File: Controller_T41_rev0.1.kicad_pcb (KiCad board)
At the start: 2 copper layers, 23 parts, among them J1 RJ45, J2 RJ45, J3 RJ45, J4 RJ45, J5 RJ45, J6 RJ45, J7 RJ45, J8 RJ45, J9 Screw_Terminal_01x02, U1 74HC245, U2 74HC245, U3 Teensy4.1, U4 74HC245, U5 74HC245

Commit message: Changes to be committed: 	modified:   Controller_T41_rev0.1.kicad_pcb 	modified:   Controller_T41_rev0.1.kicad_pcb-bak
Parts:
- moved H1 31.8 mm to (143.3, 97.4)
- moved H2 31.8 mm to (143.3, 148.1)
- moved H3 31.8 mm to (168.7, 97.4)
- moved H4 31.8 mm to (168.7, 148.2)
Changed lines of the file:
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@@
   )
   (module MountingHole:MountingHole_3mm_Pad_Via (layer F.Cu)
-    (at 175.006 97.028)
+    (at 143.256 97.409)
     (descr "Mounting Hole 3mm")
     (tags "mounting hole 3mm")
@@
   )
   (module MountingHole:MountingHole_3mm_Pad_Via (layer F.Cu)
-    (at 175.006 147.701)
+    (at 143.256 148.082)
     (descr "Mounting Hole 3mm")
     (tags "mounting hole 3mm")
@@
   )
   (module MountingHole:MountingHole_3mm_Pad_Via (layer F.Cu)
-    (at 200.406 97.028)
+    (at 168.656 97.409)
     (descr "Mounting Hole 3mm")
     (tags "mounting hole 3mm")
@@
   )
   (module MountingHole:MountingHole_3mm_Pad_Via (layer F.Cu)
-    (at 200.406 147.828)
+    (at 168.656 148.209)
     (descr "Mounting Hole 3mm")
     (tags "mounting hole 3mm")

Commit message: modified:   Controller_T41_rev0.1.kicad_pcb 	modified:   Controller_T41_rev0.1.kicad_pcb-bak 	modified:   Controller_T41_rev0.1.net 	modified:   Controller_T41_rev0.1.sch-bak 	modified:   fp-info-cache
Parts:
- moved J4 179.1 mm to (172.3, 39.5), turned to 180 degrees
- moved J3 156.4 mm to (154.2, 39.5), turned to 180 degrees
- moved J8 148.9 mm to (172.3, 192.8), turned to 0 degrees
- moved J2 127.2 mm to (185.8, 91.4), turned to 90 degrees
- moved J7 125.7 mm to (155.1, 192.8), turned to 0 degrees
- moved RN3 119.7 mm to (175.4, 154.6), turned to 270 degrees
- moved J6 113.8 mm to (185.8, 163.3), turned to 90 degrees
- moved J1 102.6 mm to (185.8, 108.7), turned to 90 degrees
- moved RN4 97.0 mm to (147.4, 153.4), turned to 270 degrees
- moved U4 95.0 mm to (155.1, 142.5), turned to 90 degrees
- moved J5 89.7 mm to (185.8, 146.1), turned to 90 degrees
- moved U2 88.1 mm to (177.9, 102.9), turned to 270 degrees
- moved RN2 87.0 mm to (175.4, 84.7), turned to 270 degrees
- moved U5 78.2 mm to (127.1, 142.5), turned to 90 degrees
- moved U3 73.4 mm to (156.1, 122.9), turned to 180 degrees
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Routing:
- net GND: track 389.7 -> 0.00 mm
- net Net-(C1-Pad2): track 174.2 -> 0.00 mm
- net Net-(J4-Pad2): track 117.0 -> 0.00 mm
- net Net-(J4-Pad4): track 112.6 -> 0.00 mm
- net Net-(J4-Pad6): track 107.9 -> 0.00 mm
- net Net-(J5-Pad2): track 107.8 -> 0.00 mm
- net Net-(J4-Pad8): track 103.5 -> 0.00 mm
- net Net-(J5-Pad4): track 103.1 -> 0.00 mm
- net Net-(J5-Pad6): track 98.4 -> 0.00 mm
- net Net-(J5-Pad8): track 93.7 -> 0.00 mm
- net Net-(J3-Pad2): track 90.7 -> 0.00 mm
- net Net-(J6-Pad2): track 86.3 -> 0.00 mm
- net Net-(J3-Pad4): track 86.0 -> 0.00 mm
- net Net-(J6-Pad4): track 81.6 -> 0.00 mm
- net Net-(J3-Pad6): track 81.3 -> 0.00 mm
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
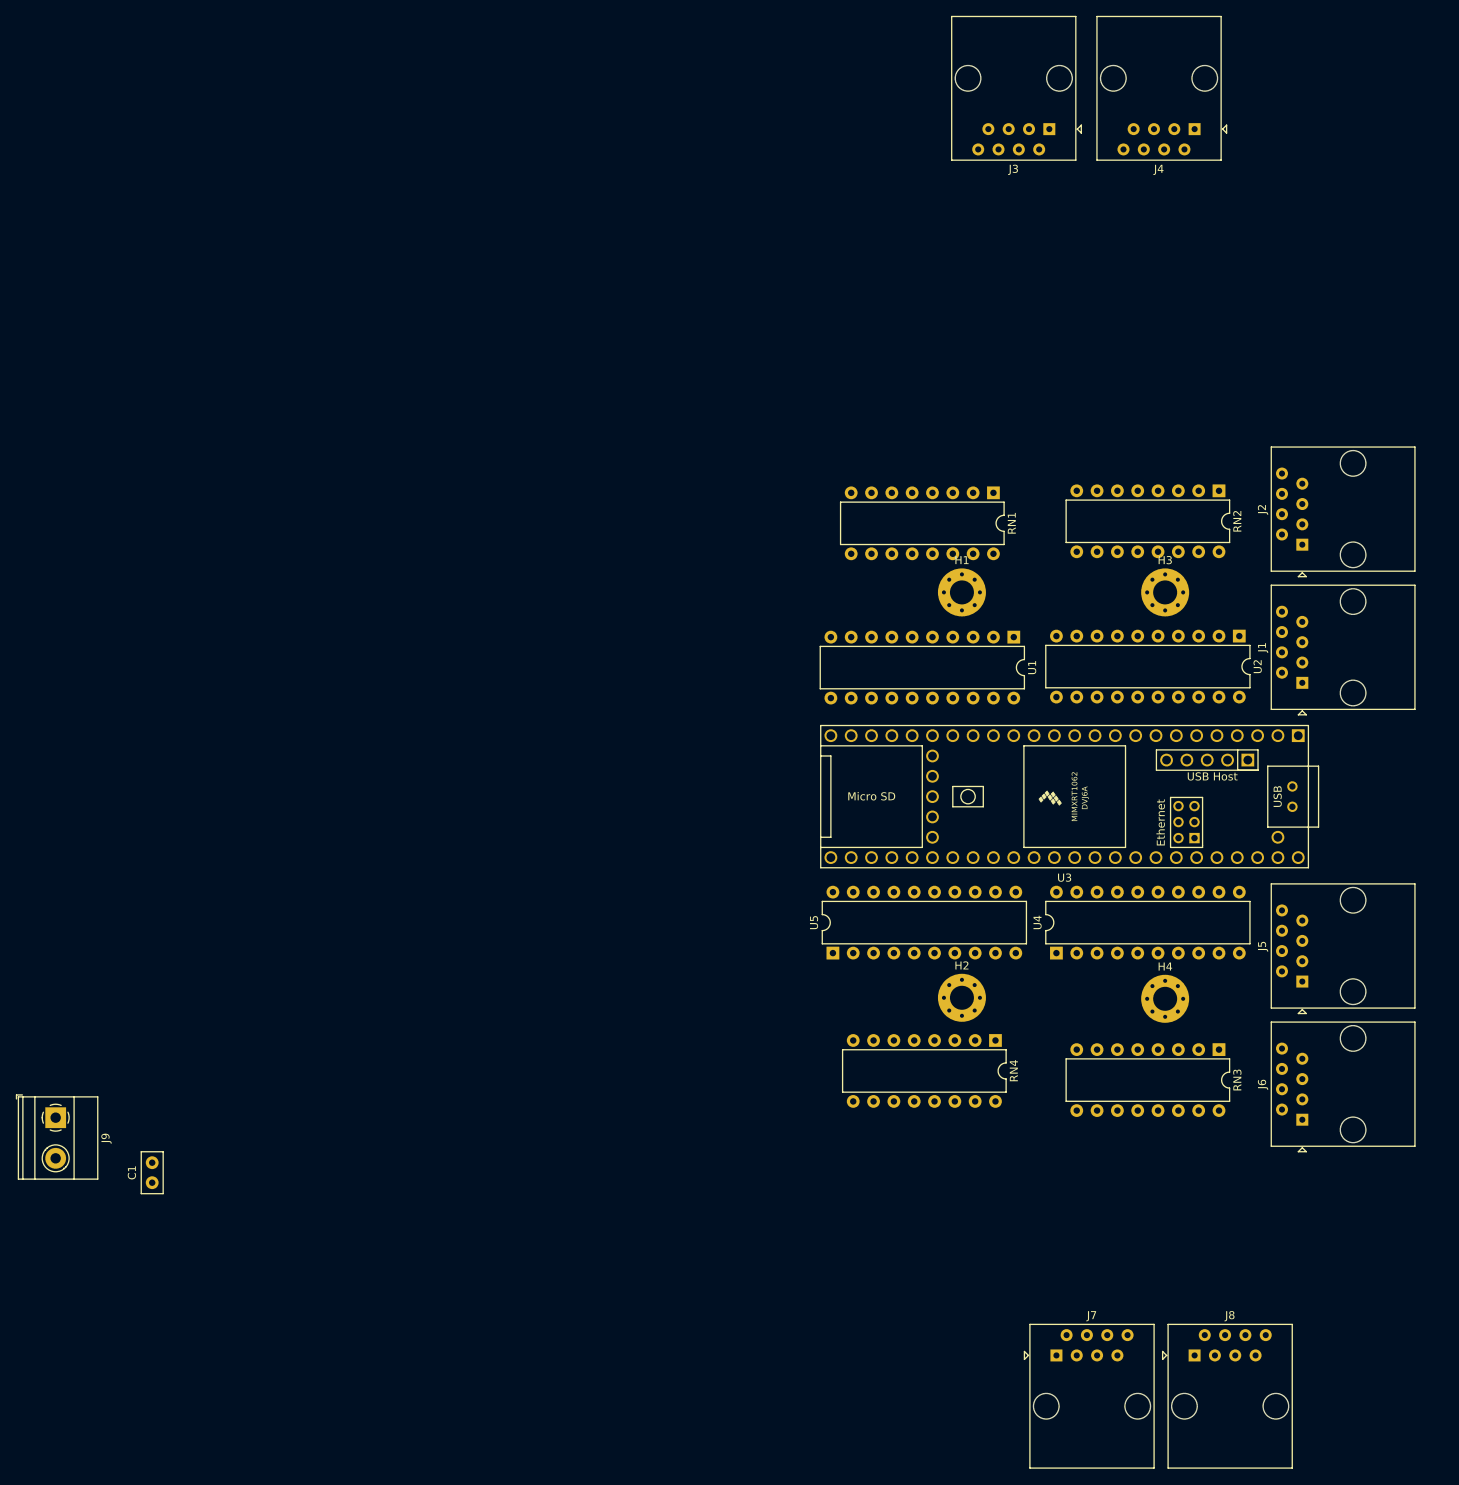
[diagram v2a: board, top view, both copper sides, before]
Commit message: updated board layout, converted rj-45 ports to dual rj-45 ports Converted design to kicad 5.
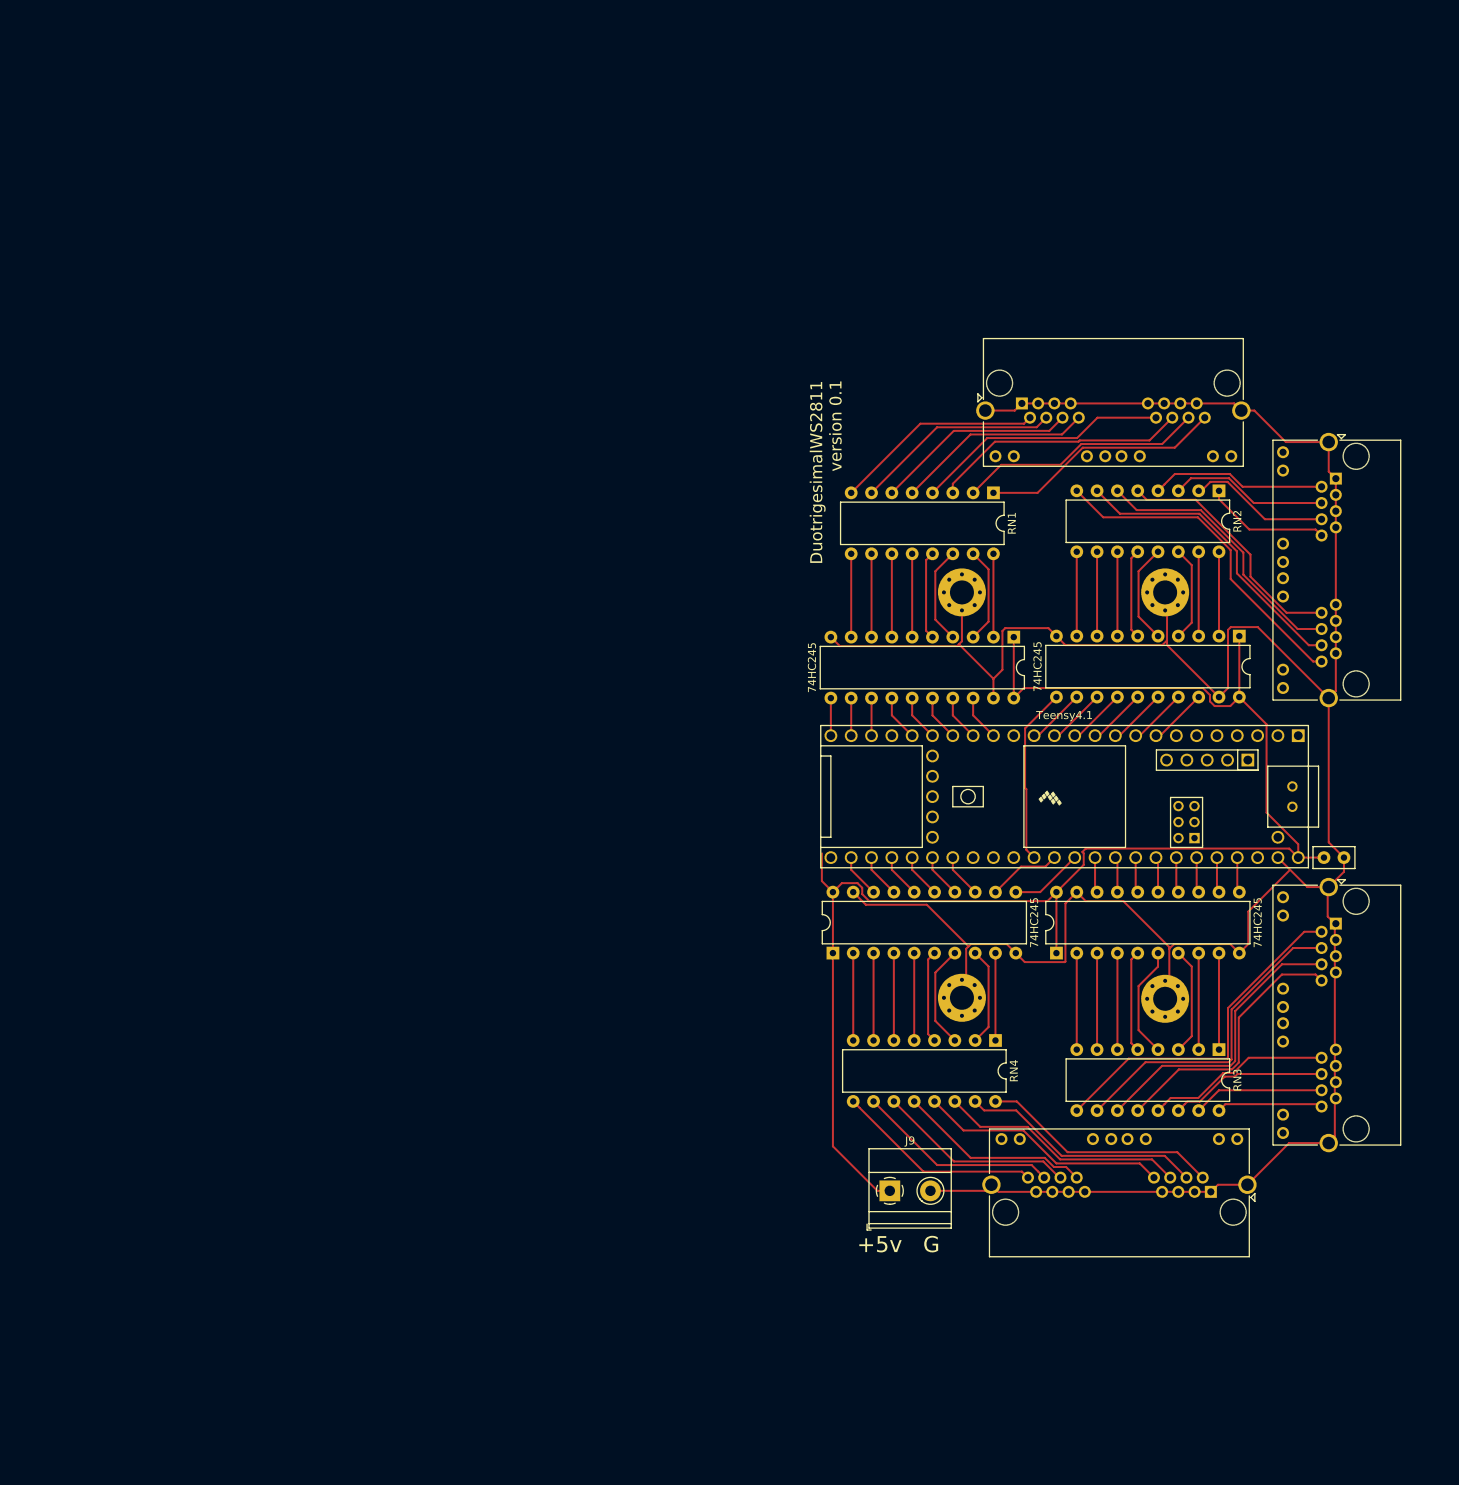
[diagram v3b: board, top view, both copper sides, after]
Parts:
- removed J5, J6, J7, J8: RJ45, Connector_RJ:RJ45_Amphenol_54602-x08_Horizontal
- J1, J2, J3, J4: value RJ45 -> RJ45_LED_Shielded_x2; footprint Connector_RJ:RJ45_Amphenol_54602-x08_Horizontal -> Connector_RJ:RJ45_Amphenol_RJHSE538X-02
- moved C1 154.4 mm to (191.0, 130.6), turned to 180 degrees
- moved J3 134.4 mm to (174.4, 172.3)
- moved J9 104.7 mm to (134.2, 172.2), turned to 0 degrees
- moved J4 100.9 mm to (190.0, 138.8), turned to 270 degrees
- moved J2 39.2 mm to (150.7, 73.8), turned to 0 degrees
- moved J1 25.9 mm to (190.0, 83.2), turned to 270 degrees
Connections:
- H2 pad 1: Net-(H2-Pad1) -> GND
- J1 pad 8: Net-(H2-Pad1) -> Net-(J1-Pad8)
- RN1 pad 1: Net-(J3-Pad8) -> Net-(J2-Pad20)
- RN1 pad 2: Net-(J3-Pad6) -> Net-(J2-Pad18)
- RN1 pad 3: Net-(J3-Pad4) -> Net-(J2-Pad16)
- RN1 pad 4: Net-(J3-Pad2) -> Net-(J2-Pad14)
- RN1 pad 5: Net-(J4-Pad8) -> Net-(J2-Pad8)
- RN1 pad 6: Net-(J4-Pad6) -> Net-(J2-Pad6)
- RN1 pad 7: Net-(J4-Pad4) -> Net-(J2-Pad4)
- RN1 pad 8: Net-(J4-Pad2) -> Net-(J2-Pad2)
- RN2 pad 1: Net-(H2-Pad1) -> Net-(J1-Pad8)
- RN2 pad 5: Net-(J2-Pad8) -> Net-(J1-Pad14)
- RN2 pad 6: Net-(J2-Pad6) -> Net-(J1-Pad16)
- RN2 pad 7: Net-(J2-Pad4) -> Net-(J1-Pad18)
- RN2 pad 8: Net-(J2-Pad2) -> Net-(J1-Pad20)
- RN3 pad 10: Net-(J6-Pad6) -> Net-(J4-Pad4)
- RN3 pad 11: Net-(J6-Pad4) -> Net-(J4-Pad6)
- RN3 pad 12: Net-(J6-Pad2) -> Net-(J4-Pad8)
- RN3 pad 13: Net-(J5-Pad8) -> Net-(J4-Pad14)
- RN3 pad 14: Net-(J5-Pad6) -> Net-(J4-Pad16)
- RN3 pad 15: Net-(J5-Pad4) -> Net-(J4-Pad18)
- RN3 pad 16: Net-(J5-Pad2) -> Net-(J4-Pad20)
- RN3 pad 9: Net-(J6-Pad8) -> Net-(J4-Pad2)
- RN4 pad 10: Net-(J8-Pad6) -> Net-(J3-Pad18)
- RN4 pad 11: Net-(J8-Pad4) -> Net-(J3-Pad16)
- RN4 pad 12: Net-(J8-Pad2) -> Net-(J3-Pad14)
- RN4 pad 13: Net-(J7-Pad8) -> Net-(J3-Pad8)
- RN4 pad 14: Net-(J7-Pad6) -> Net-(J3-Pad6)
- RN4 pad 15: Net-(J7-Pad4) -> Net-(J3-Pad4)
- RN4 pad 16: Net-(J7-Pad2) -> Net-(J3-Pad2)
- RN4 pad 9: Net-(J8-Pad8) -> Net-(J3-Pad20)
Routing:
- net GND: track 0.00 -> 387.8 mm
- net Net-(C1-Pad2): track 0.00 -> 190.8 mm
- net Net-(J4-Pad2): track 0.00 -> 43.5 mm
- net Net-(J1-Pad20): track 0.00 -> 41.6 mm
- net Net-(J4-Pad4): track 0.00 -> 40.1 mm
- net Net-(J1-Pad18): track 0.00 -> 37.7 mm
- net Net-(J4-Pad6): track 0.00 -> 36.8 mm
- net Net-(J1-Pad16): track 0.00 -> 34.3 mm
- net Net-(J4-Pad8): track 0.00 -> 33.6 mm
- net Net-(J2-Pad16): track 0.00 -> 32.0 mm
- net Net-(J2-Pad14): track 0.00 -> 31.8 mm
- net Net-(J3-Pad8): track 0.00 -> 31.4 mm
- net Net-(J1-Pad14): track 0.00 -> 30.9 mm
- net Net-(J3-Pad6): track 0.00 -> 30.9 mm
- net Net-(J2-Pad18): track 0.00 -> 30.8 mm
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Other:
- board text added: "+5v"
- board text added: "DuotrigesimalWS2811"
- board text added: "G"
- board text added: "version 0.1"

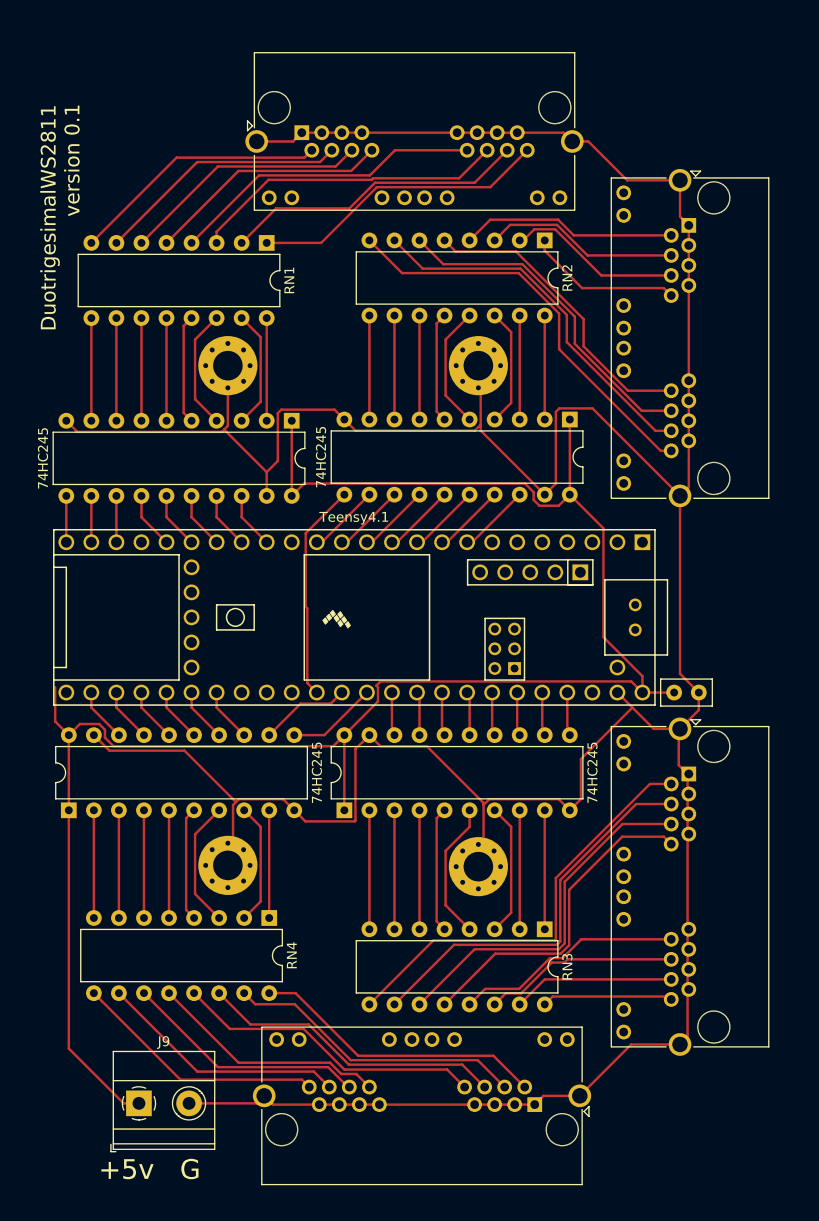
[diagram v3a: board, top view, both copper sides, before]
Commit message: modified:   Controller_T41_rev0.1.kicad_pcb Added board outline.
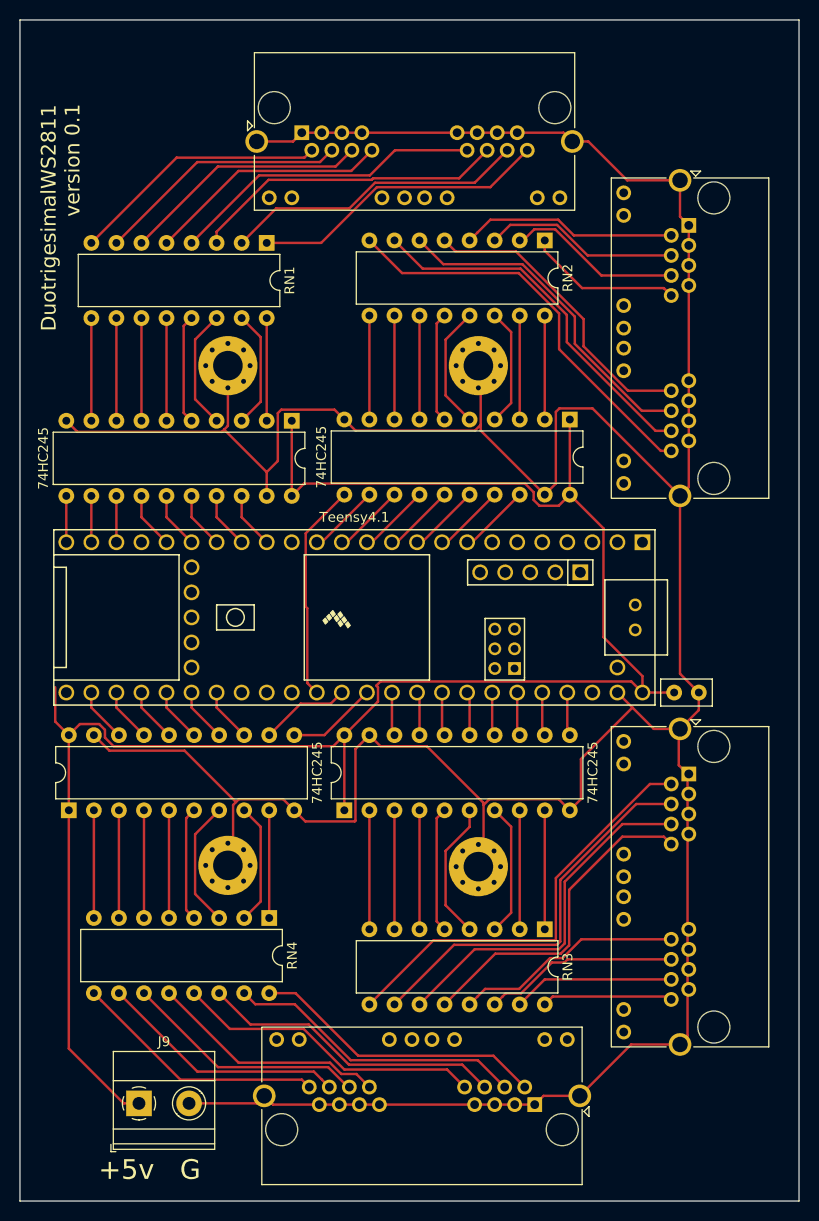
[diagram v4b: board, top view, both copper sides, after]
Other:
- board outline added: 79 x 119.8 mm
